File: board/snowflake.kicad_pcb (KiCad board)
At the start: 2 copper layers, 129 x 148.8 mm, 84 parts, among them J1 Conn_01x02_Pin, J3 TC2030, U1 TZ-5050S2RGB-5V-I4-H1, U10 TZ-5050S2RGB-5V-I4-H1, U11 TZ-5050S2RGB-5V-I4-H1, U12 TZ-5050S2RGB-5V-I4-H1, U13 TZ-5050S2RGB-5V-I4-H1, U14 TZ-5050S2RGB-5V-I4-H1, U15 TZ-5050S2RGB-5V-I4-H1, U16 TZ-5050S2RGB-5V-I4-H1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

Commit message: Submitted for production
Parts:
- moved R2 1.96 mm to (151.8, 170.7)
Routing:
- net GND: track 69.8 -> 71.0 mm, vias 66 -> 67

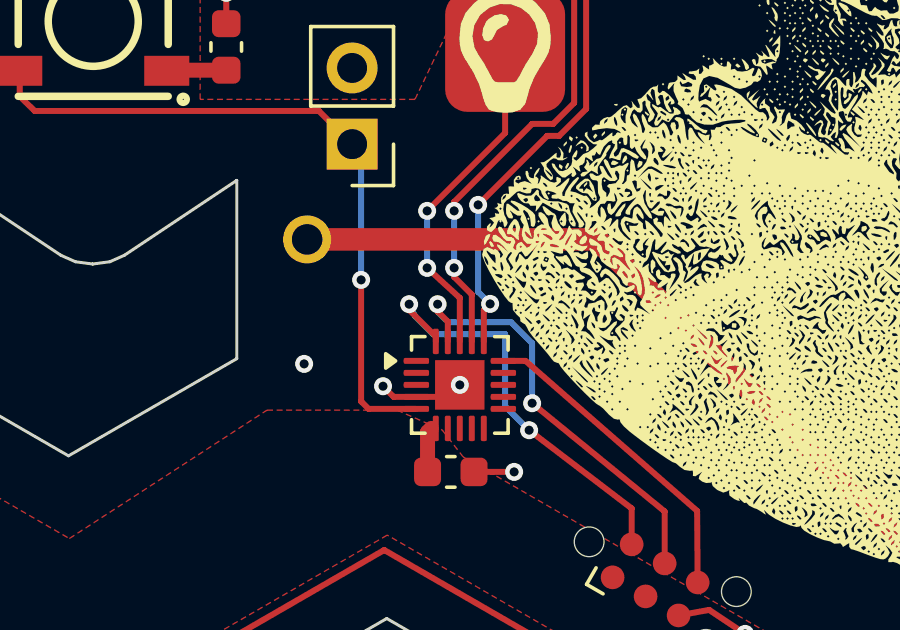
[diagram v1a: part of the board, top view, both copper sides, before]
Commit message: Add missing 3d file for CH32v003 footprint
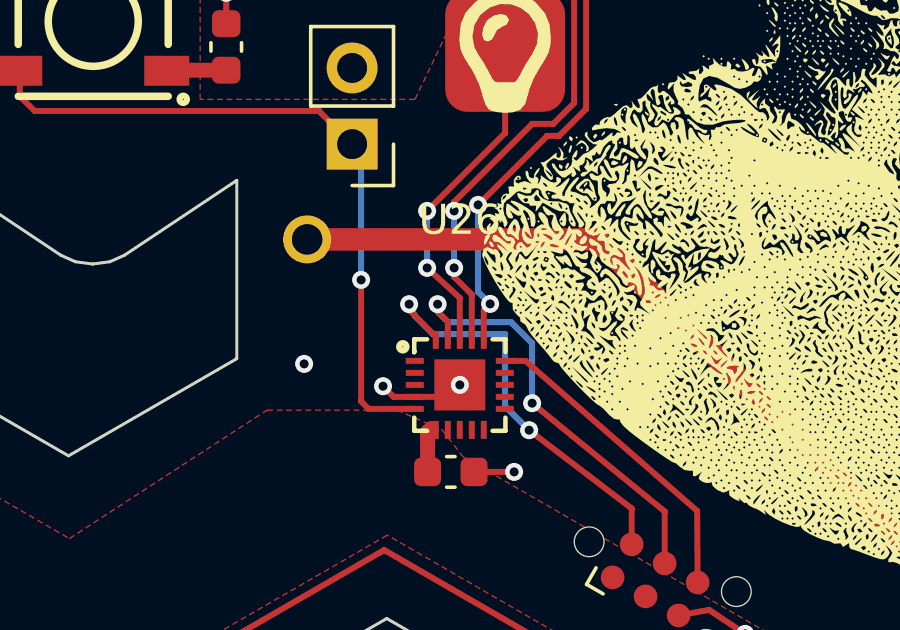
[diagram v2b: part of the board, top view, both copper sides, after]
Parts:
- U26: footprint Package_DFN_QFN:QFN-20-1EP_3x3mm_P0.4mm_EP1.65x1.65mm -> easyeda2kicad:QFN-20_L3.0-W3.0-P0.40-TL-EP1.7
